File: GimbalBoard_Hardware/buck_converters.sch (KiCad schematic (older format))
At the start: 7 parts

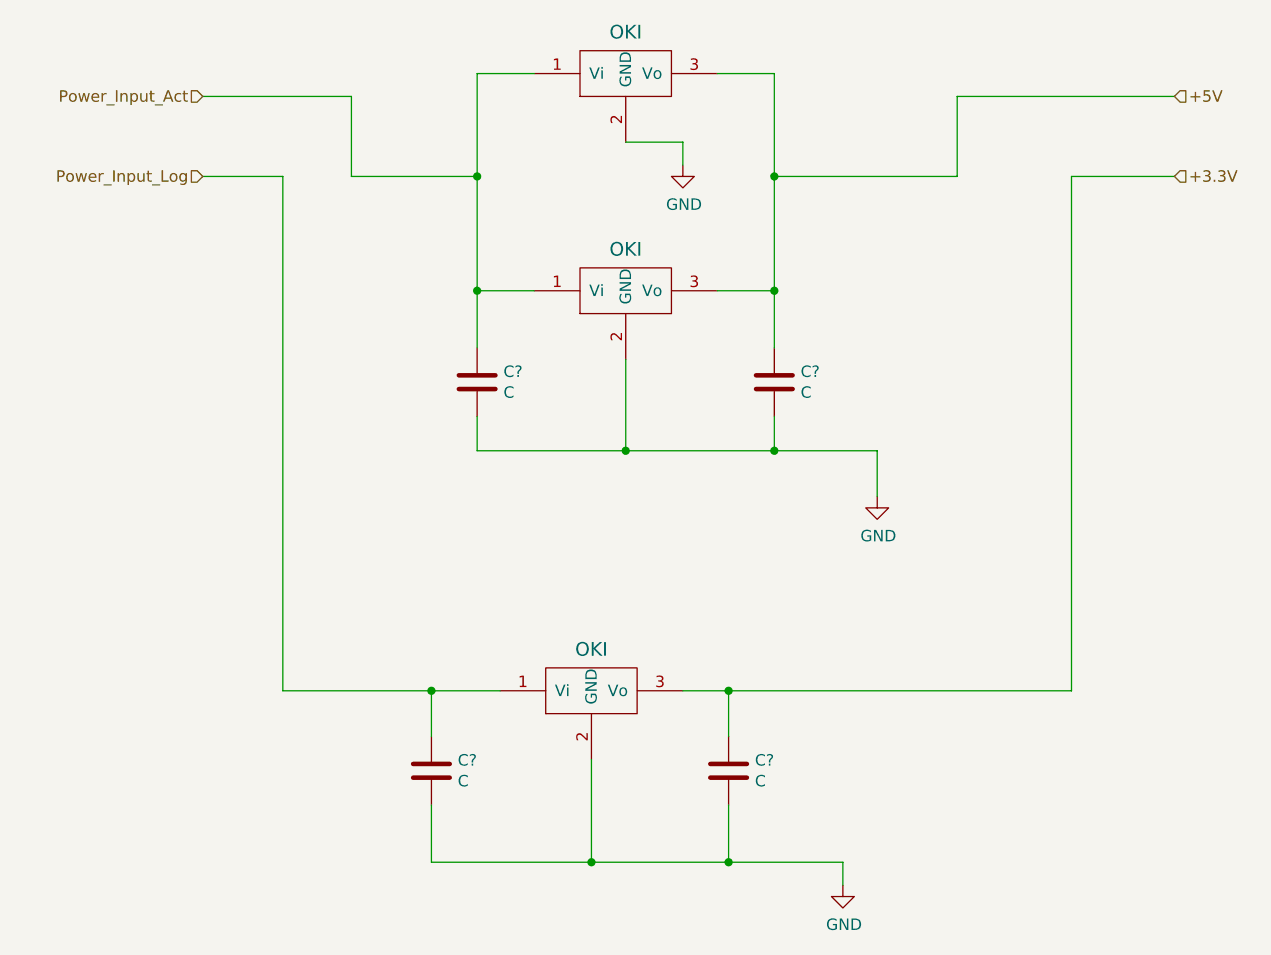
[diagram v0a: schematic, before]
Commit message: made buck converter sheet less ugly
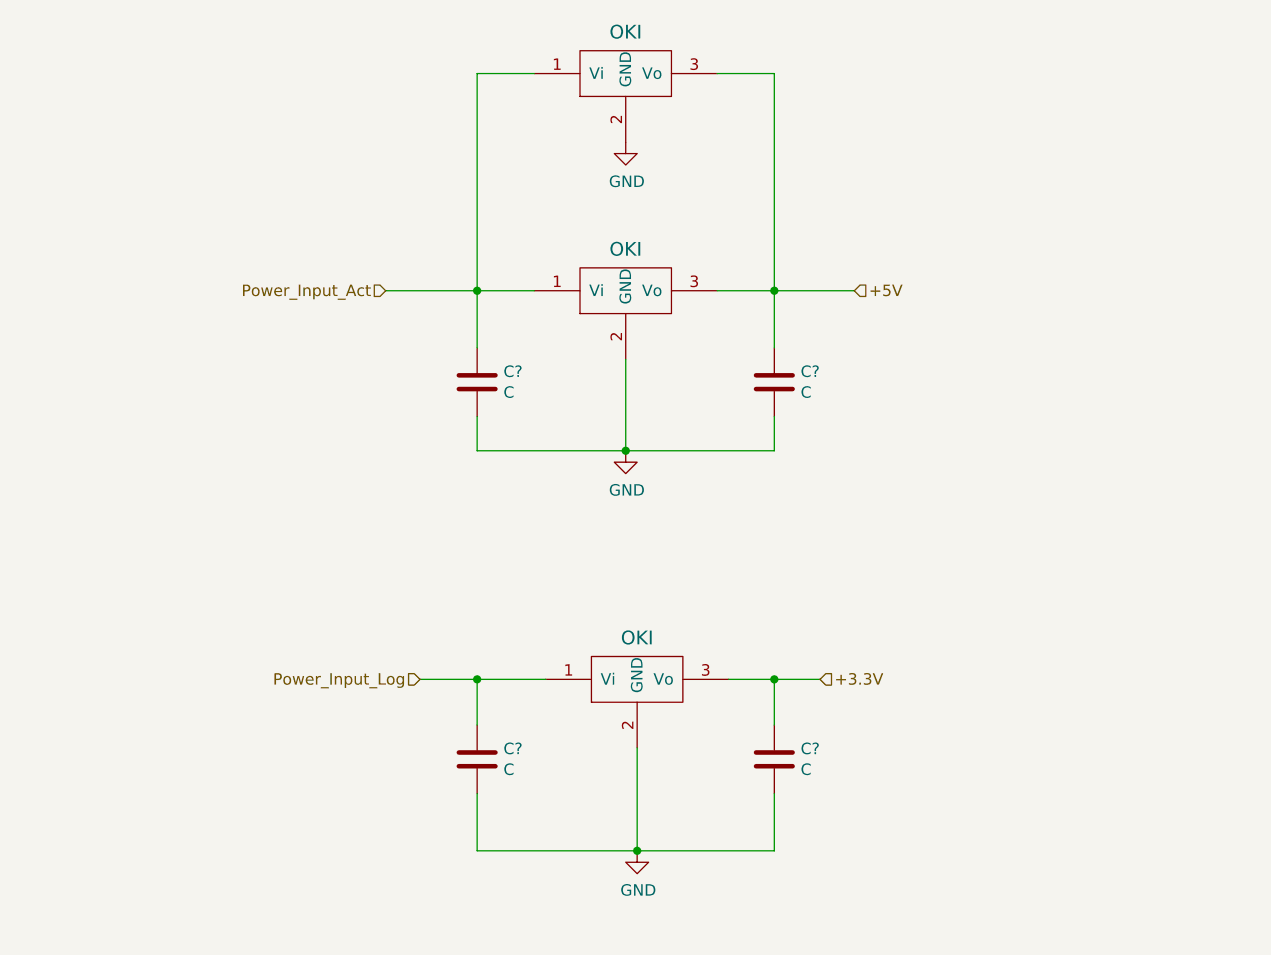
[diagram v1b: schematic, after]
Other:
- moved on the sheet: C?
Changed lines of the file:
@@
 L power:GND #PWR?
 U 1 1 615DD8CE
-P 4300 1950
+P 4050 1850
 AR Path="/615DD8CE" Ref="#PWR?"  Part="1"
 AR Path="/615B83A4/615DD8CE" Ref="#PWR?"  Part="1"
-F 0 "#PWR?" H 4300 1700 50  0001 C CNN
-F 1 "GND" H 4305 1777 50  0000 C CNN
-F 2 "" H 4300 1950 50  0001 C CNN
-F 3 "" H 4300 1950 50  0001 C CNN
-	1    4300 1950
+F 0 "#PWR?" H 4050 1600 50  0001 C CNN
+F 1 "GND" H 4055 1677 50  0000 C CNN
+F 2 "" H 4050 1850 50  0001 C CNN
+F 3 "" H 4050 1850 50  0001 C CNN
+	1    4050 1850
 	1    0    0    -1
 $EndComp
@@
 L Device:C C?
 U 1 1 615DD904
-P 3200 4600
+P 3400 4550
 AR Path="/615DD904" Ref="C?"  Part="1"
 AR Path="/615B83A4/615DD904" Ref="C?"  Part="1"
-F 0 "C?" H 3315 4646 50  0000 L CNN
-F 1 "C" H 3315 4555 50  0000 L CNN
-F 2 "" H 3238 4450 50  0001 C CNN
-F 3 "~" H 3200 4600 50  0001 C CNN
-	1    3200 4600
+F 0 "C?" H 3515 4596 50  0000 L CNN
+F 1 "C" H 3515 4505 50  0000 L CNN
+F 2 "" H 3438 4400 50  0001 C CNN
+F 3 "~" H 3400 4550 50  0001 C CNN
+	1    3400 4550
 	1    0    0    -1
 $EndComp
@@
 L Device:C C?
 U 1 1 615DD90A
-P 4500 4600
+P 4700 4550
 AR Path="/615DD90A" Ref="C?"  Part="1"
 AR Path="/615B83A4/615DD90A" Ref="C?"  Part="1"
-F 0 "C?" H 4615 4646 50  0000 L CNN
-F 1 "C" H 4615 4555 50  0000 L CNN
-F 2 "" H 4538 4450 50  0001 C CNN
-F 3 "~" H 4500 4600 50  0001 C CNN
-	1    4500 4600
+F 0 "C?" H 4815 4596 50  0000 L CNN
+F 1 "C" H 4815 4505 50  0000 L CNN
+F 2 "" H 4738 4400 50  0001 C CNN
+F 3 "~" H 4700 4550 50  0001 C CNN
+	1    4700 4550
 	1    0    0    -1
 $EndComp
@@
 L MRDT_Devices:OKI U?
 U 1 1 615DD910
-P 3700 4350
+P 3900 4300
 AR Path="/615DD910" Ref="U?"  Part="1"
 AR Path="/615B83A4/615DD910" Ref="U?"  Part="1"
-F 0 "U?" H 3750 4300 60  0001 C CNN
-F 1 "OKI" H 3900 4631 60  0000 C CNN
-F 2 "" H 3500 4250 60  0001 C CNN
-F 3 "" H 3500 4250 60  0001 C CNN
-	1    3700 4350
+F 0 "U?" H 3950 4250 60  0001 C CNN
+F 1 "OKI" H 4100 4581 60  0000 C CNN
+F 2 "" H 3700 4200 60  0001 C CNN
+F 3 "" H 3700 4200 60  0001 C CNN
+	1    3900 4300
 	1    0    0    -1
 $EndComp
-Text HLabel 2200 1650 0    50   Input ~ 0
+Text HLabel 3000 2500 0    50   Input ~ 0
 Power_Input_Act
-Text HLabel 2200 2000 0    50   Input ~ 0
+Text HLabel 3150 4200 0    50   Input ~ 0
 Power_Input_Log
-Text HLabel 6450 1650 2    50   Input ~ 0
+Text HLabel 5050 2500 2    50   Input ~ 0
 +5V
-Text HLabel 6450 2000 2    50   Input ~ 0
+Text HLabel 4900 4200 2    50   Input ~ 0
 +3.3V
 $Comp
 L power:GND #PWR?
 U 1 1 615E5C89
-P 5150 3400
-F 0 "#PWR?" H 5150 3150 50  0001 C CNN
-F 1 "GND" H 5155 3227 50  0000 C CNN
-F 2 "" H 5150 3400 50  0001 C CNN
-F 3 "" H 5150 3400 50  0001 C CNN
-	1    5150 3400
+P 4050 3200
+F 0 "#PWR?" H 4050 2950 50  0001 C CNN
+F 1 "GND" H 4055 3027 50  0000 C CNN
+F 2 "" H 4050 3200 50  0001 C CNN
+F 3 "" H 4050 3200 50  0001 C CNN
+	1    4050 3200
 	1    0    0    -1
 $EndComp
@@
 L power:GND #PWR?
 U 1 1 615E5D6A
-P 5000 5100
-F 0 "#PWR?" H 5000 4850 50  0001 C CNN
-F 1 "GND" H 5005 4927 50  0000 C CNN
-F 2 "" H 5000 5100 50  0001 C CNN
-F 3 "" H 5000 5100 50  0001 C CNN
-	1    5000 5100
+P 4100 4950
+F 0 "#PWR?" H 4100 4700 50  0001 C CNN
+F 1 "GND" H 4105 4777 50  0000 C CNN
+F 2 "" H 4100 4950 50  0001 C CNN
+F 3 "" H 4100 4950 50  0001 C CNN
+	1    4100 4950
 	1    0    0    -1
 $EndComp
 Wire Wire Line
-	4050 1850 4300 1850
-Wire Wire Line
-	4300 1850 4300 1950
-Wire Wire Line
 	4450 1550 4700 1550
-Wire Wire Line
-	4700 1550 4700 2000
 Wire Wire Line
 	4700 2500 4450 2500
@@
 	3650 1550 3400 1550
 Wire Wire Line
-	3400 1550 3400 2000
-Wire Wire Line
 	3400 2500 3650 2500
-Wire Wire Line
-	2200 1650 2850 1650
-Wire Wire Line
-	2850 1650 2850 2000
-Wire Wire Line
-	2850 2000 3400 2000
-Connection ~ 3400 2000
-Wire Wire Line
-	3400 2000 3400 2500
 Wire Wire Line
 	3400 2500 3400 2750
@@
 	3400 3200 4050 3200
 Wire Wire Line
-	5150 3200 5150 3400
-Wire Wire Line
 	4700 3050 4700 3200
-Connection ~ 4700 3200
-Wire Wire Line
-	4700 3200 5150 3200
 Wire Wire Line
 	4700 2750 4700 2500
@@
 	4050 3200 4700 3200
 Wire Wire Line
-	4700 2000 5500 2000
+	3400 4200 3400 4400
 Wire Wire Line
-	5500 2000 5500 1650
+	3400 4200 3700 4200
 Wire Wire Line
-	5500 1650 6450 1650
-Connection ~ 4700 2000
+	3400 4700 3400 4950
 Wire Wire Line
-	4700 2000 4700 2500
+	3400 4950 4100 4950
 Wire Wire Line
-	2200 2000 2550 2000
+	4700 4700 4700 4950
 Wire Wire Line
-	2550 2000 2550 4250
+	4100 4500 4100 4950
+Connection ~ 4100 4950
 Wire Wire Line
-	2550 4250 3200 4250
+	4100 4950 4700 4950
 Wire Wire Line
-	6000 4250 6000 2000
+	4700 4400 4700 4200
 Wire Wire Line
-	6000 2000 6450 2000
+	4500 4200 4700 4200
 Wire Wire Line
-	3200 4250 3200 4450
-Connection ~ 3200 4250
+	4700 1550 4700 2500
 Wire Wire Line
-	3200 4250 3500 4250
+	3400 1550 3400 2500
 Wire Wire Line
-	3200 4750 3200 5000
+	4700 2500 5050 2500
 Wire Wire Line
-	3200 5000 3900 5000
+	3000 2500 3400 2500
 Wire Wire Line
-	5000 5000 5000 5100
+	3150 4200 3400 4200
+Connection ~ 3400 4200
 Wire Wire Line
-	4500 4750 4500 5000
-Connection ~ 4500 5000
-Wire Wire Line
-	4500 5000 5000 5000
-Wire Wire Line
-	3900 4550 3900 5000
-Connection ~ 3900 5000
-Wire Wire Line
-	3900 5000 4500 5000
-Wire Wire Line
-	4500 4450 4500 4250
-Wire Wire Line
-	4300 4250 4500 4250
-Connection ~ 4500 4250
-Wire Wire Line
-	4500 4250 6000 4250
+	4700 4200 4900 4200
+Connection ~ 4700 4200
 $EndSCHEMATC
